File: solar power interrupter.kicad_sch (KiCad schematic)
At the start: 18 parts, among them J1 USB_C_Receptacle_USB2.0, J2 Screw_Terminal_01x04, Q1 BSS138, Q2 BSS138, Q3 BSS84

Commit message: added protection to battery connection, changed pins on connector for safety, added zener diodes to limit Vgs, added protection for relay drive pin
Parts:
- removed R8: (no value), Resistor_SMD:R_0805_2012Metric, symbol Device:R
- added D1, D2: D_Zener, Diode_SMD:D_SOD-123, symbol Device:D_Zener
- added D3: D_TVS, Diode_SMD:D_SMB, symbol Device:D_TVS
- C1: value (none) -> 4.7u; footprint (none) -> Capacitor_SMD:C_0805_2012Metric; DST_PN (none) -> 1276-1259-1-ND
- F1: value Fuse -> USB Fuse; DST_PN (none) -> 507-1802-1-ND
- F2: value Fuse -> Batt Fuse; DST_PN (none) -> 490-4673-1-ND
- J1: DST_PN (none) -> 2073-USB4085-GF-ACT-ND
- J2: DST_PN (none) -> 277-1024-ND
- Q1, Q2: DST_PN (none) -> BSS138-TPMSCT-ND
- Q3: DST_PN (none) -> BSS84-TPMSCT-ND
- R1, R2: DST_PN (none) -> RMCF0805JT5K10CT-ND
- R3: DST_PN (none) -> 13-AC0805FR-1010KLCT-ND
- R4: value (none) -> 56k; footprint (none) -> Resistor_SMD:R_0805_2012Metric; DST_PN (none) -> RMCF0805FT56K0CT-ND
- R5: value (none) -> 56k; DST_PN (none) -> RMCF0805FT56K0CT-ND
- R6: value (none) -> 6.2K; DST_PN (none) -> RMCF0805JT6K20CT-ND
- R7: value (none) -> 2.7K; footprint (none) -> Resistor_SMD:R_0805_2012Metric; DST_PN (none) -> 2019-RK73H2ATTD2701FCT-ND
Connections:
- net +BATT: now also D2.1 (K)
- net GND: now also J2.3 (Pin_3), D1.2 (A), D3.1 (A1); no longer J2.2 (Pin_2), R7.2
- net RELAY: now also J2.2 (Pin_2), R7.2; no longer J2.3 (Pin_3), Q3.3 (D)
- net at Q3.1 (G), R5.1: now also D2.2 (A)
- net at Q1.3 (D), Q2.1 (G), R4.2: now also D1.1 (K); no longer R7.1
- new net RELAY_UNPROTECTED: D3.2 (A2), Q3.3 (D), R7.1
- no-connect marks 0 -> 6
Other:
- note added: "Battery+ Solar Relay + Battery- Solar Relay -"
- note removed: "Battery+ Battery- Solar Relay + Solar Relay -"
- moved on the sheet: J2

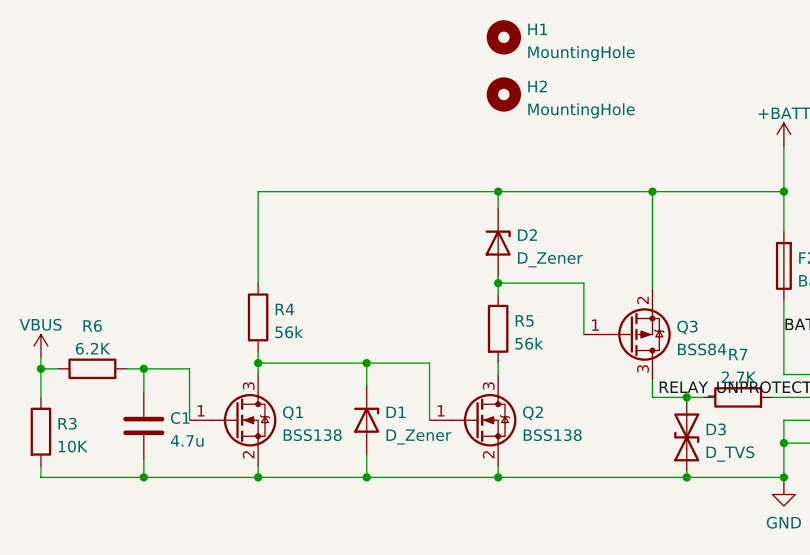
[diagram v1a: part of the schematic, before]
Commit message: updated simulation added needed pullup resistor, note this wasn't included in the PCB that I ordered. added images to readme.
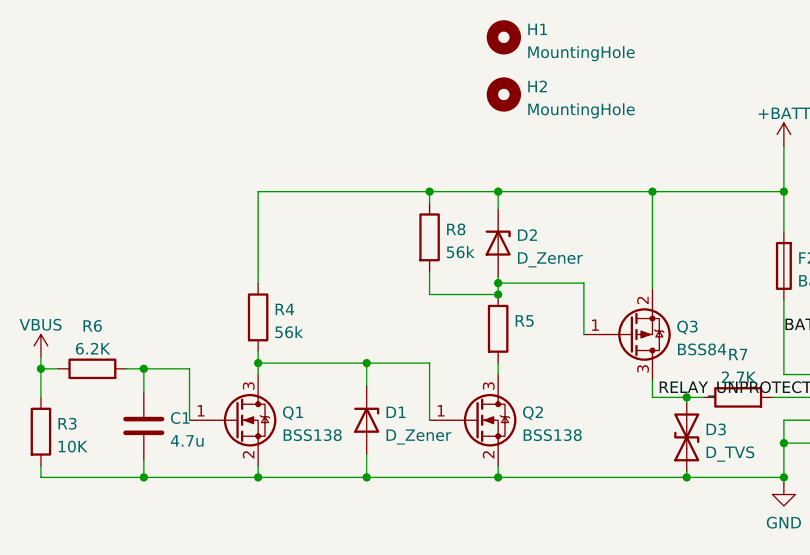
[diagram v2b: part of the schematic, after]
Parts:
- added R8: 56k, Resistor_SMD:R_0805_2012Metric, symbol Device:R
- R5: value 56k -> (none); footprint Resistor_SMD:R_0805_2012Metric -> (none); DST_PN RMCF0805FT56K0CT-ND -> 13-AC0805FR-1010KLCT-ND
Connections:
- net +BATT: now also R8.1
- net at D2.2 (A), Q3.1 (G), R5.1: now also R8.2
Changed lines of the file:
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@@
   (junction (at 158.75 77.47) (diameter 0) (color 0 0 0 0)
   )
+  (junction (at 185.42 69.85) (diameter 0) (color 0 0 0 0)
+  )
   (junction (at 185.42 90.17) (diameter 0) (color 0 0 0 0)
   )
@@
   )
   (junction (at 146.05 78.105) (diameter 0) (color 0 0 0 0)
+  )
+  (junction (at 177.8 58.42) (diameter 0) (color 0 0 0 0)
   )
   (junction (at 134.62 78.105) (diameter 0) (color 0 0 0 0)
@@
   (no_connect (at 103.505 88.265))
   (no_connect (at 103.505 80.645))
+  (wire (pts (xy 177.8 59.69) (xy 177.8 58.42))
+    (stroke (width 0) (type default) (color 0 0 0 0))
+  )
   (wire (pts (xy 170.815 87.63) (xy 170.815 90.17))
     (stroke (width 0) (type default) (color 0 0 0 0))
@@
     (stroke (width 0) (type default) (color 0 0 0 0))
   )
+  (wire (pts (xy 177.8 58.42) (xy 185.42 58.42))
+    (stroke (width 0) (type default) (color 0 0 0 0))
+  )
   (wire (pts (xy 185.42 67.945) (xy 185.42 68.58))
     (stroke (width 0) (type default) (color 0 0 0 0))
@@
     (stroke (width 0) (type default) (color 0 0 0 0))
   )
+  (wire (pts (xy 177.8 69.85) (xy 185.42 69.85))
+    (stroke (width 0) (type default) (color 0 0 0 0))
+  )
   (wire (pts (xy 217.17 90.17) (xy 217.17 90.805))
     (stroke (width 0) (type default) (color 0 0 0 0))
@@
     (stroke (width 0) (type default) (color 0 0 0 0))
   )
+  (wire (pts (xy 177.8 67.31) (xy 177.8 69.85))
+    (stroke (width 0) (type default) (color 0 0 0 0))
+  )
   (wire (pts (xy 144.145 78.105) (xy 146.05 78.105))
     (stroke (width 0) (type default) (color 0 0 0 0))
@@
     (stroke (width 0) (type default) (color 0 0 0 0))
   )
-  (wire (pts (xy 158.75 58.42) (xy 185.42 58.42))
+  (wire (pts (xy 158.75 58.42) (xy 177.8 58.42))
     (stroke (width 0) (type default) (color 0 0 0 0))
   )
@@
     (pin "1")
   )
+  (symbol (lib_id "Device:R") (at 177.8 63.5 0) (unit 1)
+    (in_bom yes) (on_board yes) (fields_autoplaced)
+    (property "Reference" "R8" (id 0) (at 179.578 62.6653 0)
+      (effects (font (size 1.27 1.27)) (justify left))
+    )
+    (property "Value" "56k" (id 1) (at 179.578 65.2022 0)
+      (effects (font (size 1.27 1.27)) (justify left))
+    )
+    (property "Footprint" "Resistor_SMD:R_0805_2012Metric" (id 2) (at 176.022 63.5 90)
+      (effects (font (size 1.27 1.27)) hide)
+    )
+    (property "Datasheet" "~" (id 3) (at 177.8 63.5 0)
+      (effects (font (size 1.27 1.27)) hide)
+    )
+    (property "DST_PN" "RMCF0805FT56K0CT-ND" (id 4) (at 177.8 63.5 0)
+      (effects (font (size 1.27 1.27)) hide)
+    )
+    (pin "1")
+    (pin "2")
+  )
   (symbol (lib_id "Device:R") (at 185.42 73.66 0) (unit 1)
     (in_bom yes) (on_board yes) (fields_autoplaced)
@@
       (effects (font (size 1.27 1.27)) (justify left))
     )
-    (property "Value" "56k" (id 1) (at 187.198 75.3622 0)
-      (effects (font (size 1.27 1.27)) (justify left))
-    )
-    (property "Footprint" "Resistor_SMD:R_0805_2012Metric" (id 2) (at 183.642 73.66 90)
+    (property "Value" "" (id 1) (at 187.198 75.3622 0)
+      (effects (font (size 1.27 1.27)) (justify left))
+    )
+    (property "Footprint" "" (id 2) (at 183.642 73.66 90)
       (effects (font (size 1.27 1.27)) hide)
     )
@@
       (effects (font (size 1.27 1.27)) hide)
     )
-    (property "DST_PN" "RMCF0805FT56K0CT-ND" (id 4) (at 185.42 73.66 0)
+    (property "DST_PN" "13-AC0805FR-1010KLCT-ND" (id 4) (at 185.42 73.66 0)
       (effects (font (size 1.27 1.27)) hide)
     )
@@
     )
     (path "/d63d48bb-8353-4f86-81fa-3af96f4dae35"
-      (reference "R5") (unit 1) (value "56k") (footprint "Resistor_SMD:R_0805_2012Metric")
+      (reference "R5") (unit 1) (value "10k") (footprint "Resistor_SMD:R_0805_2012Metric")
     )
     (path "/7f7dca97-fe5c-402a-886f-5c8b0fca1d71"
@@
       (reference "R7") (unit 1) (value "2.7K") (footprint "Resistor_SMD:R_0805_2012Metric")
     )
-  )
+    (path "/ce26a67b-8096-4ac9-9430-883e76869ef9"
+      (reference "R8") (unit 1) (value "56k") (footprint "Resistor_SMD:R_0805_2012Metric")
+    )
+  )
